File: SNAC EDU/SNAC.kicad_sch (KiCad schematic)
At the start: 48 parts, among them J1 JST-PH, J2 JST-PH, J3 USB3_A, J4 Conn_01x08_Pin, J5 Conn_01x08_Pin, J6 Conn_01x02_Pin, J7 Conn_01x05_Pin, Q1 BSS138, Q2 BSS138, Q3 BSS138, Q4 BSS138, Q5 BSS138, Q6 BSS138, Q7 BSS138, U1 SN74LVC1G3157, U2 SN74LVC1G3157, U3 SN74LVC1G3157, U4 SN74LVC1G3157, U5 SN74LVC1G3157, U6 SN74LVC1G3157, U7 SN74LVC1G3157

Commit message: Made schematic notations clearer
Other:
- note added: "3.3V OR 5V LOGIC SWITCH JUMPER 5V = NO JUMPER 3.3V = JUMPER"
- note added: "HV DEBUG BREAKOUT"
- note added: "LV DEBUG BREAKOUT"
- note added: "MISC DEBUG BREAKOUT"
- note added: "PLAYER 1"
- note added: "PLAYER 2"
- note removed: "3.3V AND 5V LOGIC SWITCH JUMPER 5V = NO JUMPER 3.3V = JUMPER"
- note removed: "DEBUG BREAKOUT"

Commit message: Reassigned LV lines for match the new pinning of the PSX breakout
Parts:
- removed J1, J2: JST-PH, Connector_JST:JST_PH_S9B-PH-SM4-TB_1x09-1MP_P2.00mm_Horizontal, symbol Connector_Generic_MountingPin:Conn_01x09_MountingPin
- removed JP1, JP11, JP12, JP13, JP2: Jumper_2_Bridged, Jumper:SolderJumper-2_P1.3mm_Bridged_Pad1.0x1.5mm, symbol Jumper:Jumper_2_Bridged
- added J2: Conn_01x10_MountingPin, symbol Connector_Generic_MountingPin:Conn_01x10_MountingPin
- JP10, JP3, JP4, JP5, JP6, JP7, JP9: now left out of the parts list
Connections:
- net +3.3V: now also J2.2 (Pin_2)
- net +7.5V: now also J2.1 (Pin_1)
- net ACK: now also JP7.1 (A), J2.7 (Pin_7); no longer JP3.1 (A), JP9.2 (B)
- net ATT1: now also JP3.1 (A), J2.3 (Pin_3)
- net ATT2: now also JP4.1 (A), J2.4 (Pin_4); no longer JP5.1 (A)
- net CLK: now also JP5.1 (A), J2.5 (Pin_5); no longer JP6.1 (A)
- net CMD: now also JP9.1 (A), J2.8 (Pin_8); no longer JP4.1 (A)
- net D+: now also U2.4 (A); no longer U4.4 (A)
- net D-: now also U1.4 (A); no longer U2.4 (A)
- net DAT: now also JP6.1 (A), J2.6 (Pin_6)
- net DRAIN: now also U7.4 (A); no longer U3.4 (A)
- net HV1: no longer U1.1 (B2)
- net HV2: now also Q3.3 (D), R6.2; no longer Q2.3 (D), R4.2, U2.1 (B2)
- net HV3: now also Q4.3 (D), R8.2; no longer Q3.3 (D), R6.2, U3.1 (B2)
- net HV4: now also Q7.3 (D), R14.2; no longer Q4.3 (D), R8.2, U4.1 (B2)
- net HV5: now also Q2.3 (D), R4.2; no longer Q5.3 (D), R10.2, U5.1 (B2)
- net HV6: no longer U6.1 (B2)
- net HV7: now also Q5.3 (D), R10.2; no longer Q7.3 (D), R14.2, U7.1 (B2)
- net IRQ10: now also JP10.1 (A), J2.9 (Pin_9); no longer JP10.2 (B), JP7.1 (A)
- net LV1: now also JP9.2 (B); no longer U1.3 (B1)
- net LV2: now also JP3.2 (B), Q3.2 (S), R5.2; no longer Q2.2 (S), R3.2, U2.3 (B1)
- net LV3: now also JP7.2 (B), Q4.2 (S), R7.2; no longer JP3.2 (B), Q3.2 (S), R5.2, U3.3 (B1)
- net LV4: now also Q7.2 (S), R13.2; no longer Q4.2 (S), R7.2, U4.3 (B1)
- net LV5: now also JP6.2 (B), Q2.2 (S), R3.2; no longer JP5.2 (B), Q5.2 (S), R9.2, U5.3 (B1)
- net LV6: now also JP5.2 (B); no longer JP6.2 (B), U6.3 (B1)
- net LV7: now also JP10.2 (B), Q5.2 (S), R9.2; no longer JP7.2 (B), Q7.2 (S), R13.2, U7.3 (B1)
- net RX+: now also U4.4 (A); no longer U5.4 (A)
- net TX+: now also U6.4 (A); no longer U7.4 (A)
- net TX-: now also U5.4 (A); no longer U1.4 (A)
- net RX- renamed X-
- net X-: now also U3.4 (A); no longer U6.4 (A)
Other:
- note added: "INPUT FROM CONTROLLER BREAKOUT"
- note removed: "INPUT FROM CONTROLLER BREAKOUTS"
- note removed: "PLAYER 1"
- note removed: "PLAYER 2"
- moved on the sheet: J3, Q4, Q5, Q6, Q7, R10, R11, R12, R13, R14, R7, R8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

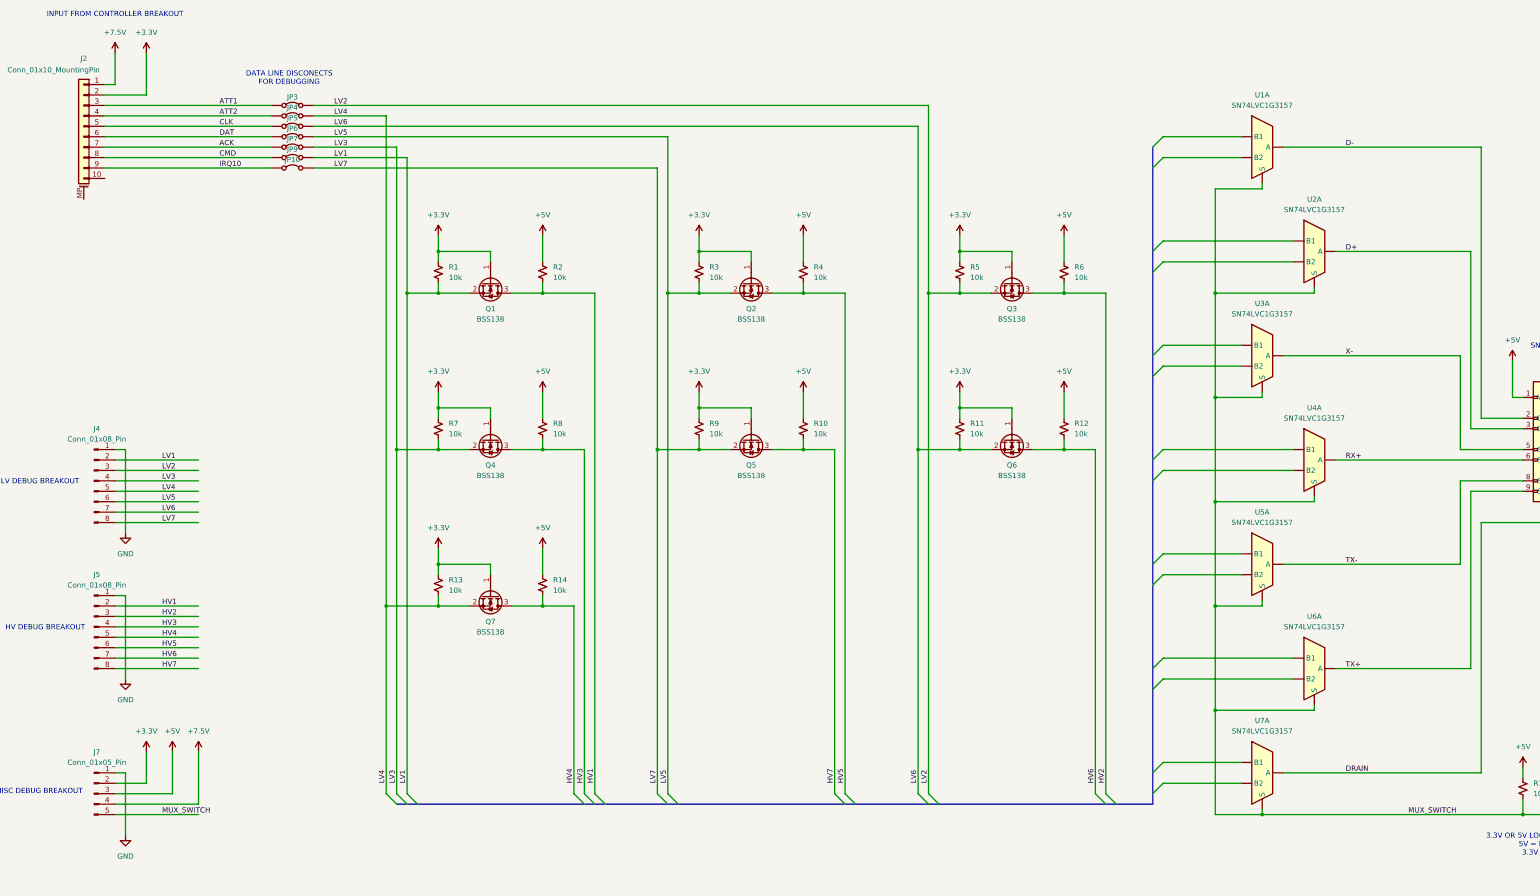
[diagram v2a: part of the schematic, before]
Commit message: renamed PS1 files to PSX
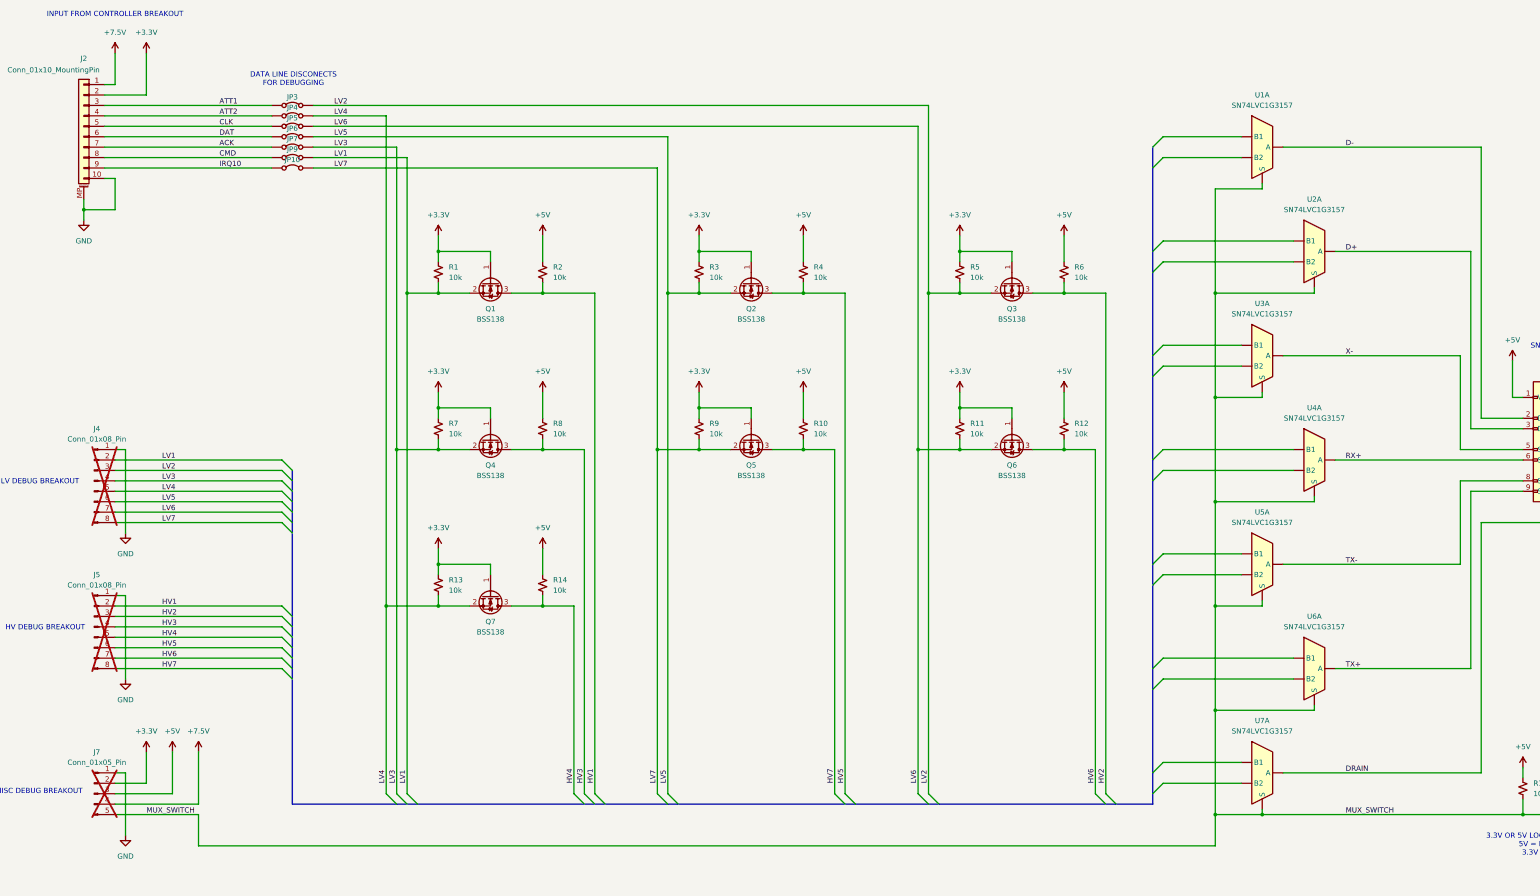
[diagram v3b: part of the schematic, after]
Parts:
- J4, J5, J7: now not fitted
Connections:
- net GND: now also J2.10 (Pin_10), J2.MP (MountPin)

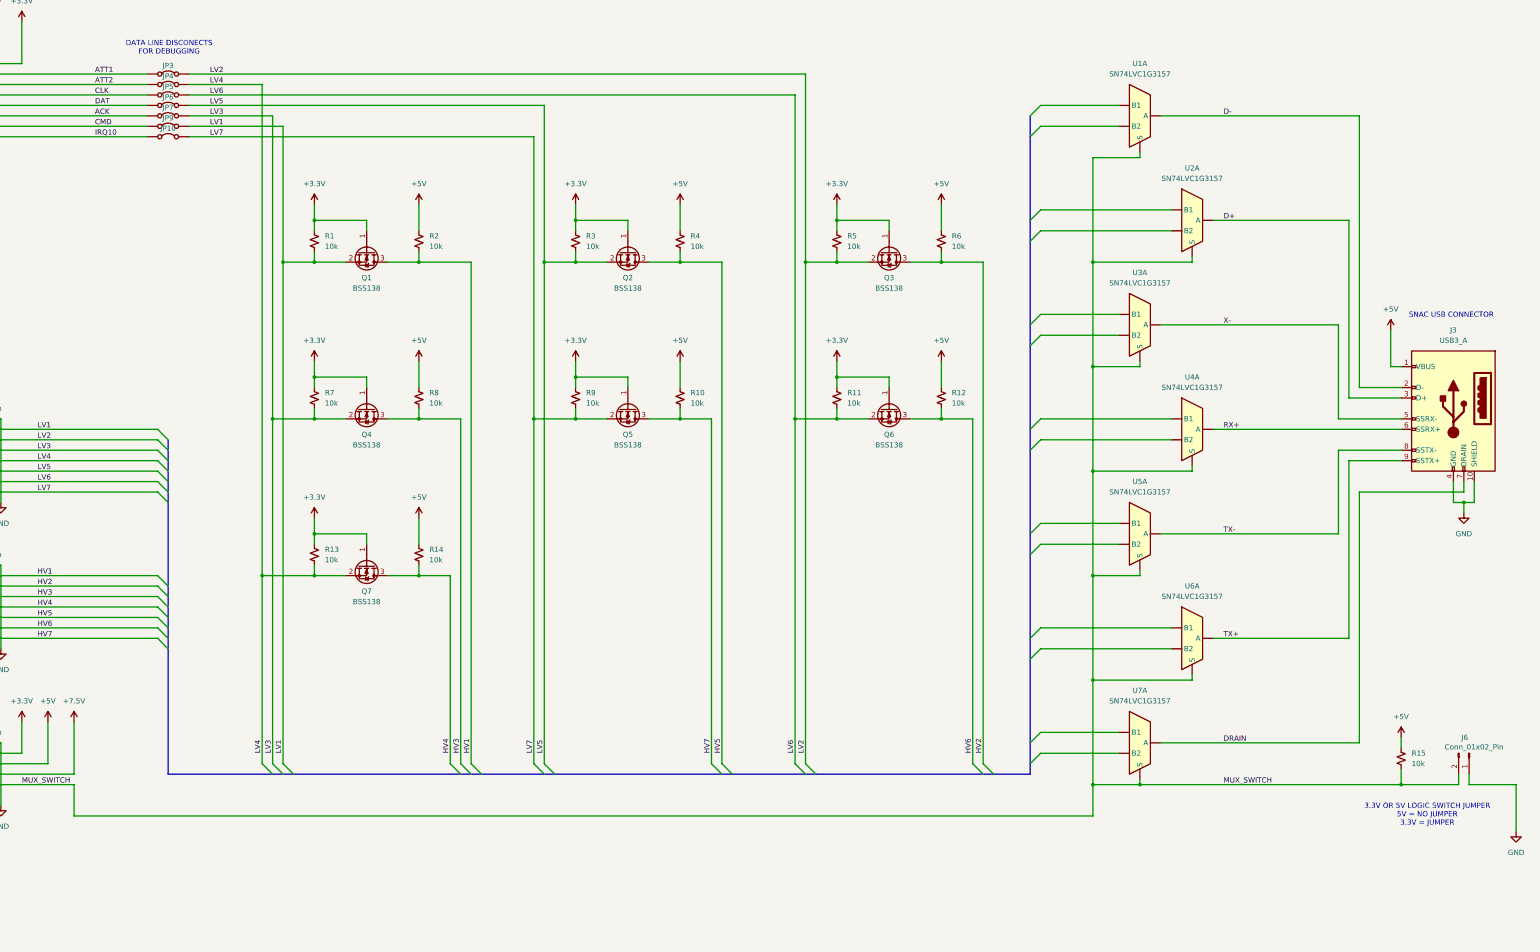
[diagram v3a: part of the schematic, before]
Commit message: Assigned data lines to switches and added 5v and 3.3v logic led indicators
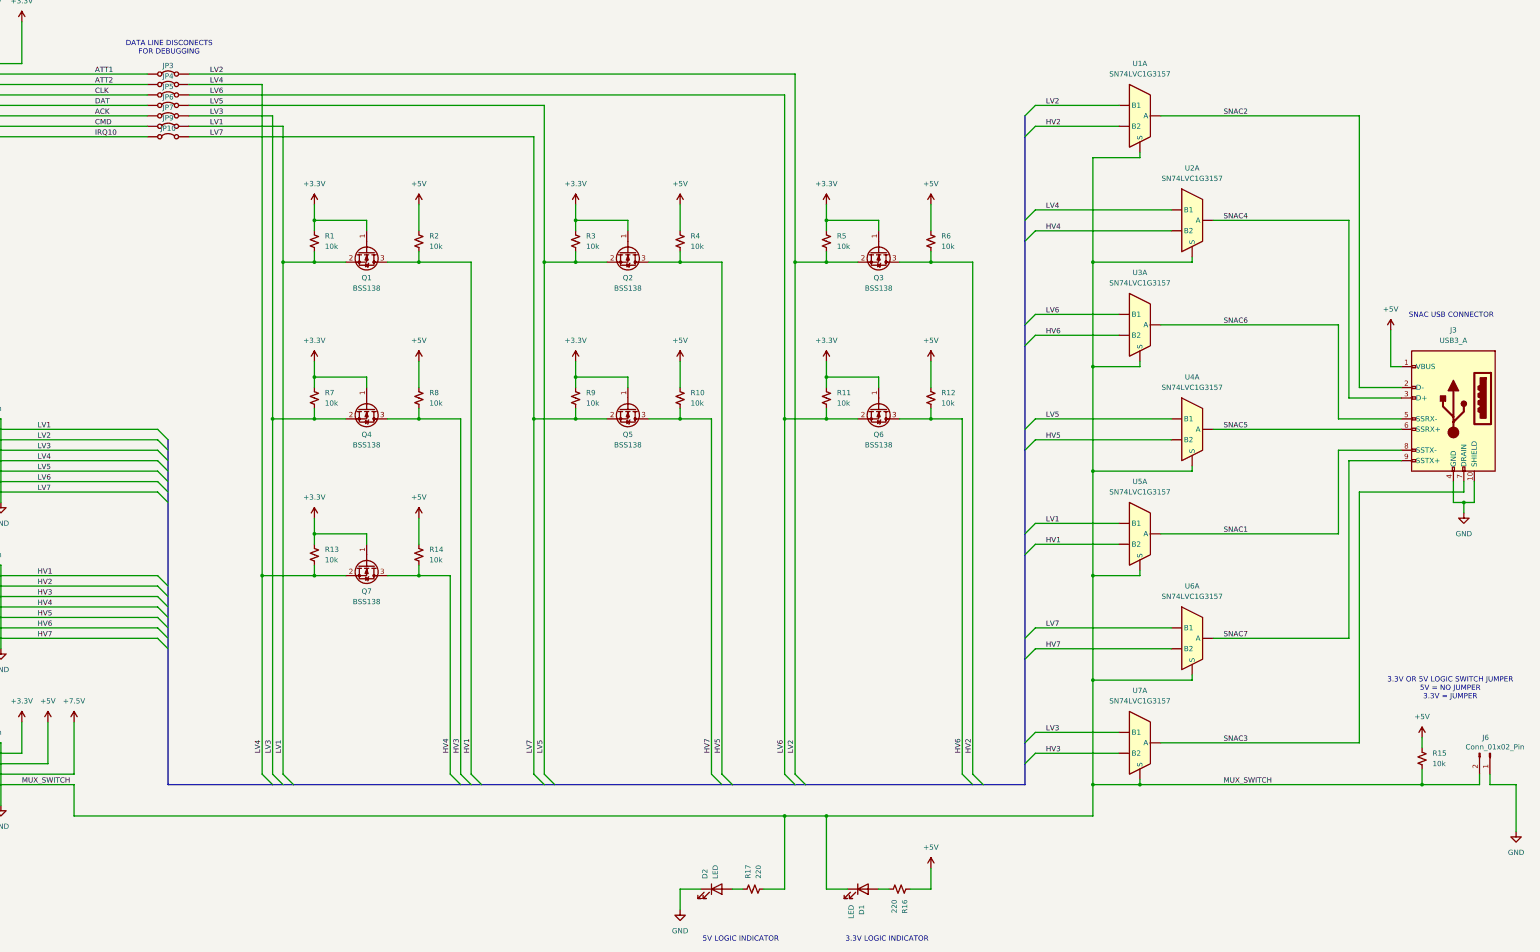
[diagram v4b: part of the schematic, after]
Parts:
- added D1, D2: LED, LED_SMD:LED_0603_1608Metric, symbol Device:LED
- added R16, R17: 220, Resistor_SMD:R_0603_1608Metric, symbol Device:R_Small_US
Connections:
- net +5V: now also R16.1
- net GND: now also D2.1 (K)
- net HV1: now also U5.1 (B2)
- net HV2: now also U1.1 (B2)
- net HV3: now also U7.1 (B2)
- net HV4: now also U2.1 (B2)
- net HV5: now also U4.1 (B2)
- net HV6: now also U3.1 (B2)
- net HV7: now also U6.1 (B2)
- net LV1: now also U5.3 (B1)
- net LV2: now also U1.3 (B1)
- net LV3: now also U7.3 (B1)
- net LV4: now also U2.3 (B1)
- net LV5: now also U4.3 (B1)
- net LV6: now also U3.3 (B1)
- net LV7: now also U6.3 (B1)
- net MUX_SWITCH: now also D1.1 (K), R17.2
- net D+ renamed SNAC4
- net D- renamed SNAC2
- net DRAIN renamed SNAC3
- net RX+ renamed SNAC5
- net TX+ renamed SNAC7
- net TX- renamed SNAC1
- net X- renamed SNAC6
- new net: D1.2 (A), R16.2
- new net: D2.2 (A), R17.1
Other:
- note added: "3.3V LOGIC INDICATOR"
- note added: "5V LOGIC INDICATOR"
- moved on the sheet: J6, Q3, Q6, R11, R12, R15, R5, R6

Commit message: assigned footprints
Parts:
- J2: footprint (none) -> Connector_JST:JST_PH_S10B-PH-SM4-TB_1x10-1MP_P2.00mm_Horizontal
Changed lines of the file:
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@@
 			)
 		)
-		(property "Footprint" ""
+		(property "Footprint" "Connector_JST:JST_PH_S10B-PH-SM4-TB_1x10-1MP_P2.00mm_Horizontal"
 			(at 35.56 48.26 0)
 			(hide yes)

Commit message: started layout
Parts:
- renumbered J2 to J1, J3 to J2, J4 to J3, J5 to J4, J7 to J5
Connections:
- net GND: now also J2.SH (SHIELD); no longer J2.10 (SHIELD)
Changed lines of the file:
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@@
 		(in_pos_files yes)
 		(dnp no)
-		(property "Reference" "J2"
+		(property "Reference" "J1"
 			(at 35.56 31.75 0)
 			(show_name no)
@@
 			(project "SNAC EDU"
 				(path "/cbd92933-d20e-42b7-906c-813e5f34c94a/fbfcc61c-380e-426e-8388-ba29034c9159"
-					(reference "J2")
+					(reference "J1")
 					(unit 1)
 				)
@@
 		(dnp yes)
 		(fields_autoplaced yes)
-		(property "Reference" "J5"
+		(property "Reference" "J4"
 			(at 38.735 157.48 0)
 			(show_name no)
@@
 			(project "SNAC EDU"
 				(path "/cbd92933-d20e-42b7-906c-813e5f34c94a/fbfcc61c-380e-426e-8388-ba29034c9159"
-					(reference "J5")
+					(reference "J4")
 					(unit 1)
 				)
@@
 		(dnp yes)
 		(fields_autoplaced yes)
-		(property "Reference" "J7"
+		(property "Reference" "J5"
 			(at 38.735 200.66 0)
 			(show_name no)
@@
 			(project "SNAC EDU"
 				(path "/cbd92933-d20e-42b7-906c-813e5f34c94a/fbfcc61c-380e-426e-8388-ba29034c9159"
-					(reference "J7")
+					(reference "J5")
 					(unit 1)
 				)
@@
 		(dnp no)
 		(fields_autoplaced yes)
-		(property "Reference" "J3"
-			(at 398.78 105.41 0)
+		(property "Reference" "J2"
+			(at 410.21 123.8249 0)
 			(show_name no)
 			(do_not_autoplace no)
@@
 					(size 1.27 1.27)
 				)
+				(justify right)
 			)
 		)
 		(property "Value" "USB3_A"
-			(at 398.78 107.95 0)
+			(at 410.21 126.3649 0)
 			(show_name no)
 			(do_not_autoplace no)
@@
 					(size 1.27 1.27)
 				)
+				(justify right)
 			)
 		)
@@
 		(pin "3"
 		)
-		(pin "10"
+		(pin "SH"
 		)
 		(pin "1"
@@
 			(project "SNAC EDU"
 				(path "/cbd92933-d20e-42b7-906c-813e5f34c94a/fbfcc61c-380e-426e-8388-ba29034c9159"
-					(reference "J3")
+					(reference "J2")
 					(unit 1)
 				)
@@
 		(dnp yes)
 		(fields_autoplaced yes)
-		(property "Reference" "J4"
+		(property "Reference" "J3"
 			(at 38.735 121.92 0)
 			(show_name no)
@@
 			(project "SNAC EDU"
 				(path "/cbd92933-d20e-42b7-906c-813e5f34c94a/fbfcc61c-380e-426e-8388-ba29034c9159"
-					(reference "J4")
+					(reference "J3")
 					(unit 1)
 				)

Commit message: continued routing
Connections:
- net +7.5V renamed +7.6V
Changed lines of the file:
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@@
 		(in_pos_files yes)
 		(dnp no)
-		(fields_autoplaced yes)
 		(property "Reference" "#PWR024"
 			(at 63.5 204.47 0)
@@
 			)
 		)
-		(property "Value" "+7.5V"
-			(at 63.5 195.58 0)
-			(show_name no)
-			(do_not_autoplace no)
-			(effects
-				(font
-					(size 1.27 1.27)
-				)
+		(property "Value" "+7.6V"
+			(at 60.198 195.58 0)
+			(show_name no)
+			(do_not_autoplace no)
+			(effects
+				(font
+					(size 1.27 1.27)
+				)
+				(justify right)
 			)
 		)
@@
 			)
 		)
-		(property "Value" "+7.5V"
+		(property "Value" "+7.6V"
 			(at 43.18 25.4 0)
 			(show_name no)
